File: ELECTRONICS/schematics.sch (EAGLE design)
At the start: 3 parts, among them IC1 LM324D, IC2 7414D

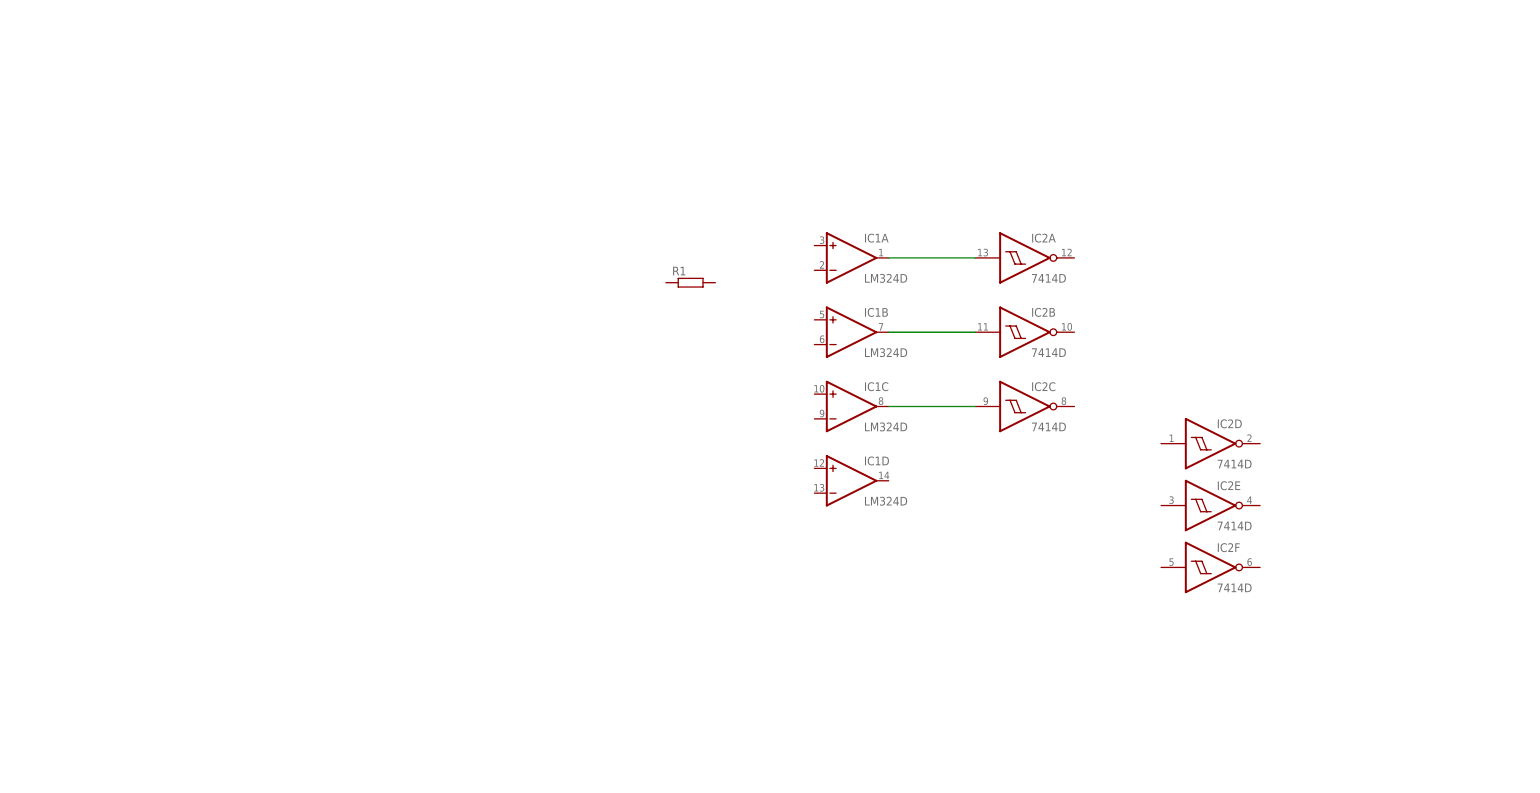
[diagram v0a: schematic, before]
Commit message: Accelerometer and ADC is created and the circuit design is started
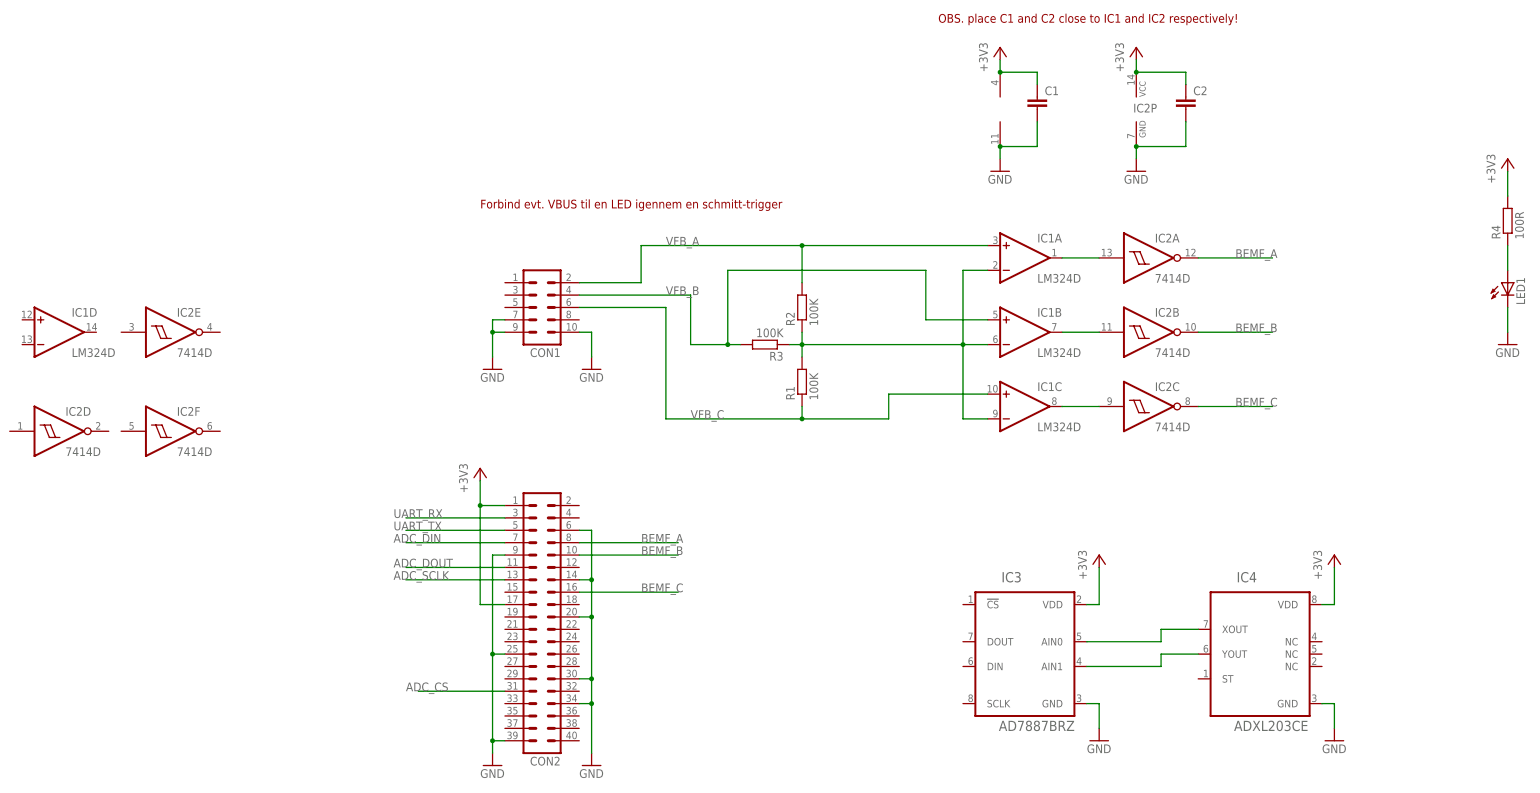
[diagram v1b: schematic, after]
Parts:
- added C1, C2: (no value), rcl:C-EUC0805K
- added CON1: (no value), con-lstb:MA05-2
- added CON2: (no value), con-lstb:MA20-2
- added IC3: AD7887BRZ, tobylib:AD7887BRZ
- added IC4: ADXL203CE, tobylib:ADXL203CE
- added LED1: (no value), led:LEDCHIP-LED0805
- added R2, R3: 100K, rcl:R-EU_R0805
- added R4: 100R, rcl:R-EU_R0805
- R1: value (none) -> 100K
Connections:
- new net +3V3: C1.1, C2.1, CON2.1, CON2.17, IC1P.V+, IC2P.VCC, IC3.VDD, IC4.VDD, R4.2
- new net ADC_CS: CON2.31
- new net ADC_DIN: CON2.7
- new net ADC_DOUT: CON2.11
- new net ADC_SCLK: CON2.13
- new net BEMF_A: CON2.8, IC2A.O
- new net BEMF_B: CON2.10, IC2B.O
- new net BEMF_C: CON2.16, IC2C.O
- new net GND: C1.2, C2.2, CON1.10, CON1.7, CON1.9, CON2.14, CON2.20, CON2.25, CON2.30, CON2.34, CON2.39, CON2.6, CON2.9, IC1P.V-, IC2P.GND, IC3.GND, IC4.GND, LED1.C
- new net N$4: IC1A.-IN, IC1B.-IN, IC1C.-IN, R1.2, R2.1, R3.1
- new net N$5: IC3.AIN0, IC4.XOUT
- new net N$6: IC3.AIN1, IC4.YOUT
- new net N$7: LED1.A, R4.1
- new net UART_RX: CON2.3
- new net UART_TX: CON2.5
- new net VFB_A: CON1.2, IC1A.+IN, R2.2
- new net VFB_B: CON1.4, IC1B.+IN, R3.2
- new net VFB_C: CON1.6, IC1C.+IN, R1.1
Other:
- note added: "Forbind evt. VBUS til en LED igennem en schmitt-trigger"
- note added: "OBS. place C1 and C2 close to IC1 and IC2 respectively!"
- moved on the sheet: IC1A, IC1B, IC1C, IC1D, IC2A, IC2B, IC2C, IC2D, IC2E, IC2F, R1
